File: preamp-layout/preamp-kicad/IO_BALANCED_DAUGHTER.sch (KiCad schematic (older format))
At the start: 49 parts, among them J29 XLR3, J30 XLR3, J31 Conn_01x03_Male, J32 Conn_01x03_Male, J33 Conn_01x03_Female, J34 Conn_01x03_Male, J35 XLR3, J36 XLR3, U6 TL072, U7 TL072, U8 TL072

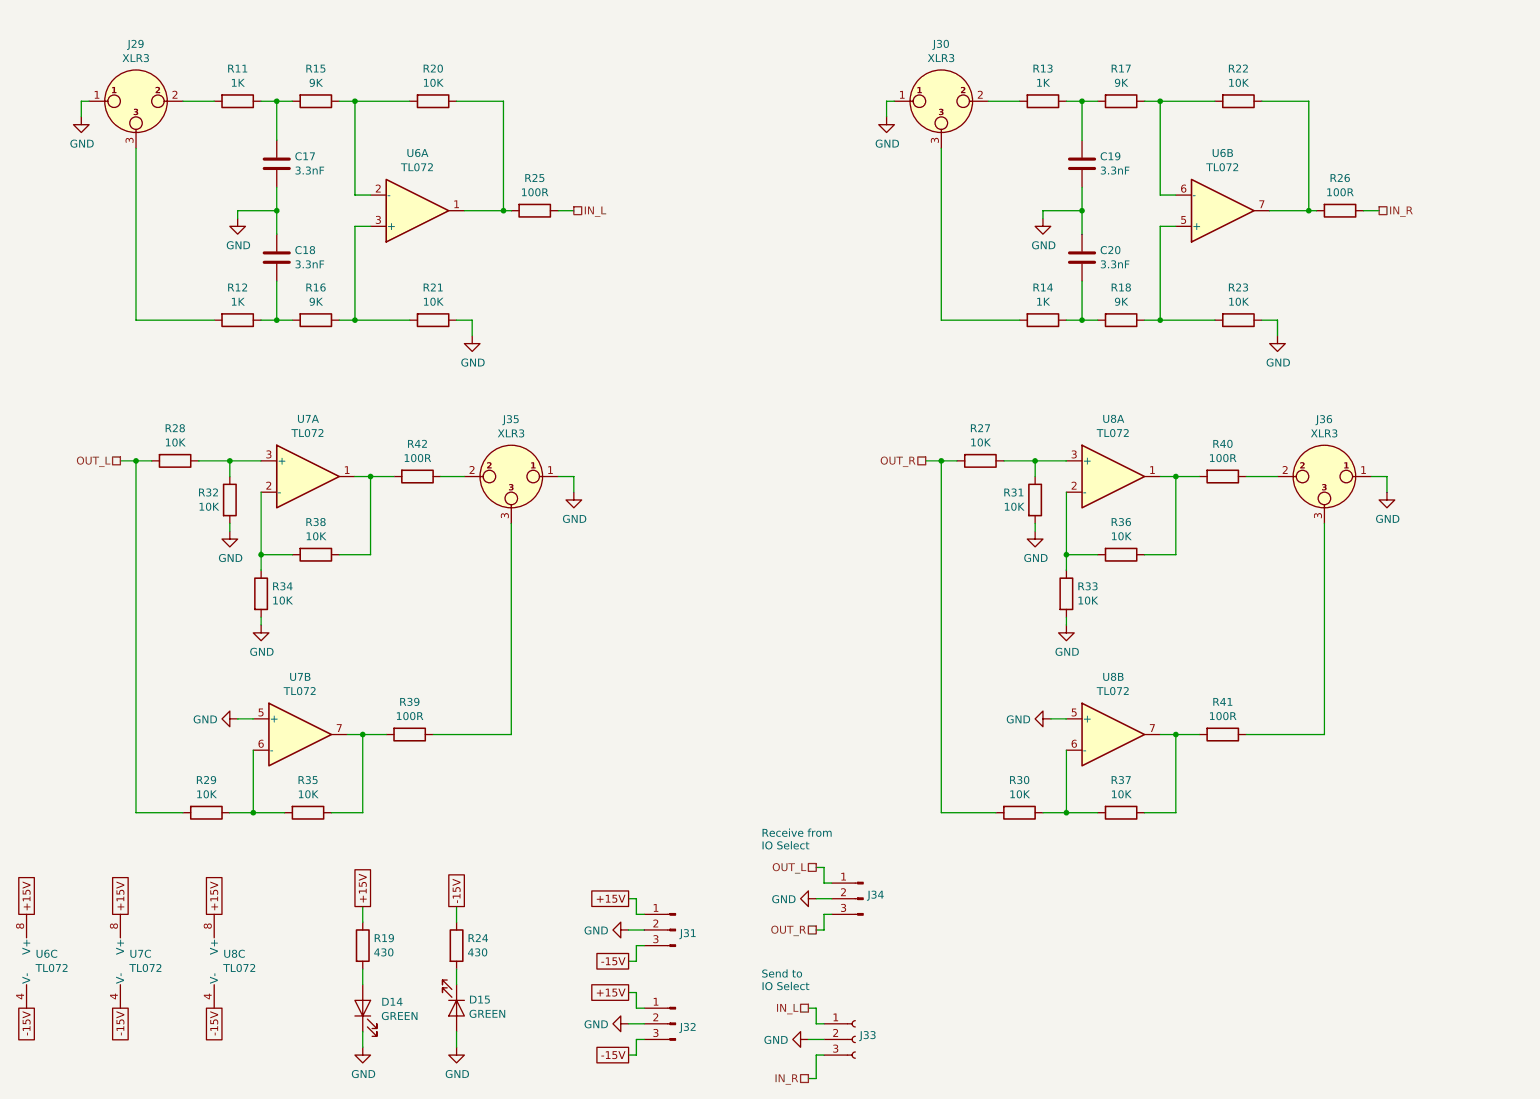
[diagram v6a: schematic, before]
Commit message: LED resistor update
In the process of reviewing layouts and associated parts sourcing, I realized that I had incorrectly calculated the resistors needed for the power supply LEDs on all boards. Updated BOM and schematics to match. Other minor schematic updates.
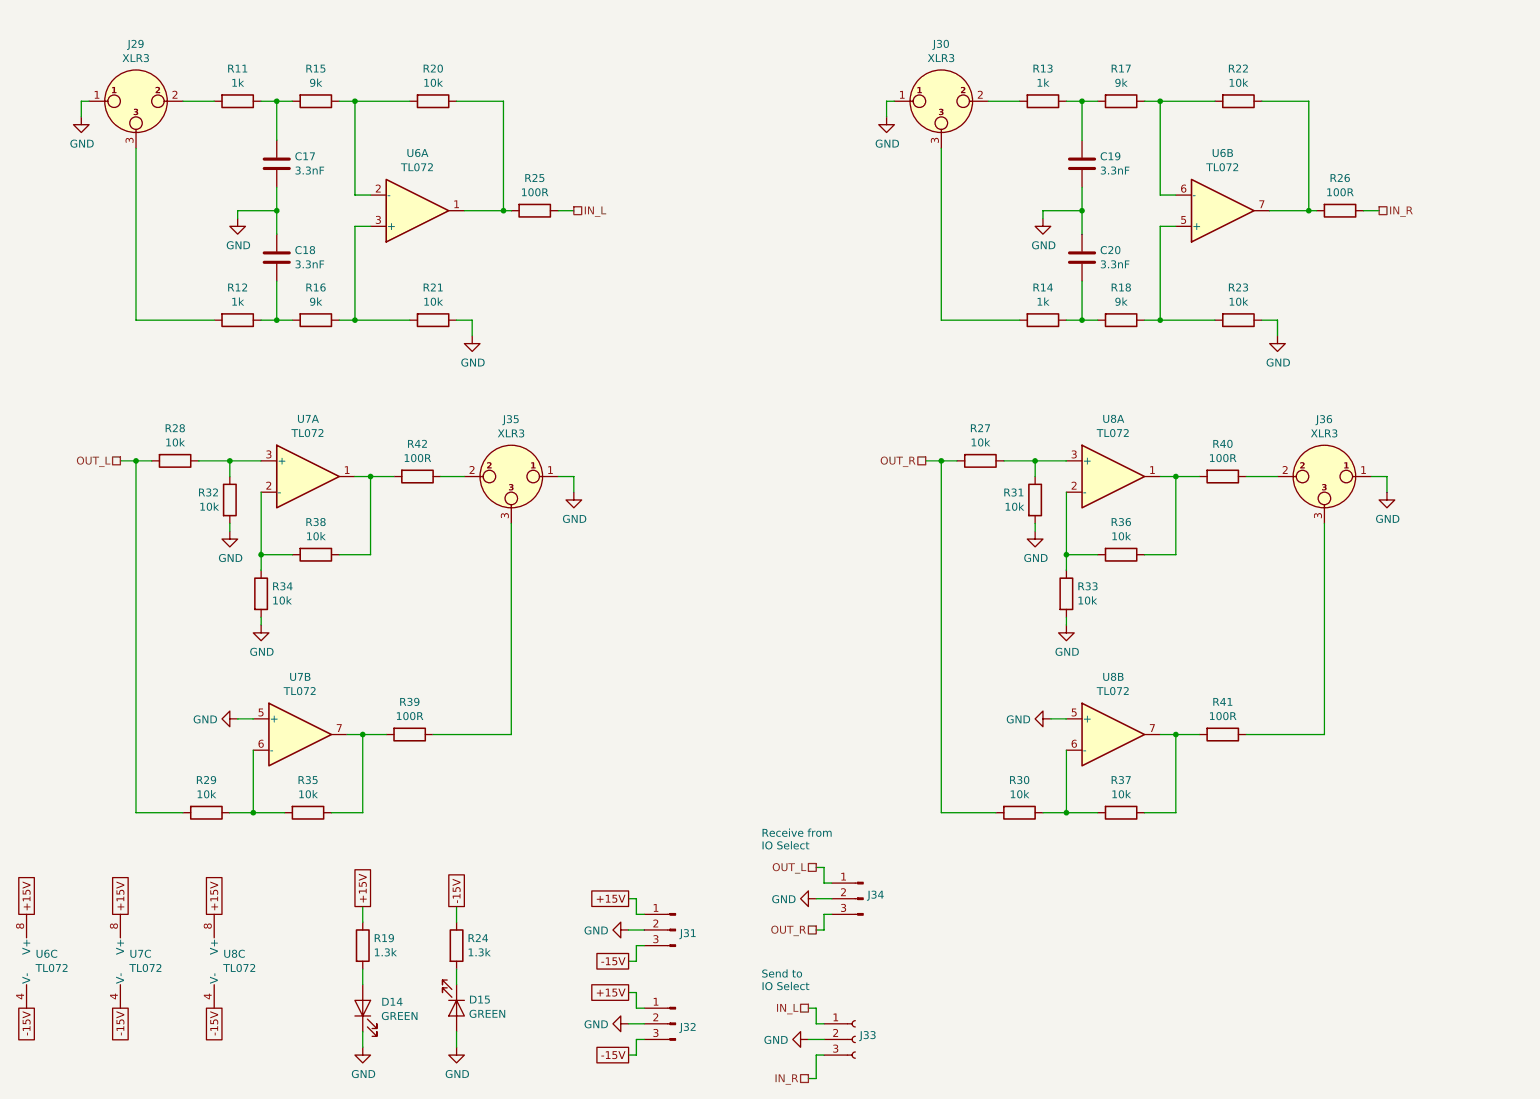
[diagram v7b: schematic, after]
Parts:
- R11, R12, R13, R14: value 1K -> 1k
- R15, R16, R17, R18: value 9K -> 9k
- R19, R24: value 430 -> 1.3k
- R20, R21, R22, R23, R27, R28, R29, R30, R31, R32, R33, R34, R35, R36, R37, R38: value 10K -> 10k
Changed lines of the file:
@@
 AR Path="/5E80BFEC/5E1BDDF0" Ref="R?"  Part="1"
 F 0 "R21" V 3493 2650 50  0000 C CNN
-F 1 "10K" V 3584 2650 50  0000 C CNN
+F 1 "10k" V 3584 2650 50  0000 C CNN
 F 2 "Resistor_SMD:R_1206_3216Metric_Pad1.42x1.75mm_HandSolder" V 3630 2650 50  0001 C CNN
 F 3 "~" H 3700 2650 50  0001 C CNN
@@
 AR Path="/5E80BFEC/5E1BDDF6" Ref="R?"  Part="1"
 F 0 "R20" V 3493 1250 50  0000 C CNN
-F 1 "10K" V 3584 1250 50  0000 C CNN
+F 1 "10k" V 3584 1250 50  0000 C CNN
 F 2 "Resistor_SMD:R_1206_3216Metric_Pad1.42x1.75mm_HandSolder" V 3630 1250 50  0001 C CNN
 F 3 "~" H 3700 1250 50  0001 C CNN
@@
 AR Path="/5E80BFEC/5E1BDE02" Ref="R?"  Part="1"
 F 0 "R16" V 2743 2650 50  0000 C CNN
-F 1 "9K" V 2834 2650 50  0000 C CNN
+F 1 "9k" V 2834 2650 50  0000 C CNN
 F 2 "Resistor_SMD:R_1206_3216Metric_Pad1.42x1.75mm_HandSolder" V 2880 2650 50  0001 C CNN
 F 3 "~" H 2950 2650 50  0001 C CNN
@@
 AR Path="/5E80BFEC/5E1BDE08" Ref="R?"  Part="1"
 F 0 "R12" V 2243 2650 50  0000 C CNN
-F 1 "1K" V 2334 2650 50  0000 C CNN
+F 1 "1k" V 2334 2650 50  0000 C CNN
 F 2 "Resistor_SMD:R_1206_3216Metric_Pad1.42x1.75mm_HandSolder" V 2380 2650 50  0001 C CNN
 F 3 "~" H 2450 2650 50  0001 C CNN
@@
 AR Path="/5E80BFEC/5E1BDE14" Ref="R?"  Part="1"
 F 0 "R11" V 2243 1250 50  0000 C CNN
-F 1 "1K" V 2334 1250 50  0000 C CNN
+F 1 "1k" V 2334 1250 50  0000 C CNN
 F 2 "Resistor_SMD:R_1206_3216Metric_Pad1.42x1.75mm_HandSolder" V 2380 1250 50  0001 C CNN
 F 3 "~" H 2450 1250 50  0001 C CNN
@@
 AR Path="/5E80BFEC/5E1BDE3B" Ref="R?"  Part="1"
 F 0 "R15" V 2743 1250 50  0000 C CNN
-F 1 "9K" V 2834 1250 50  0000 C CNN
+F 1 "9k" V 2834 1250 50  0000 C CNN
 F 2 "Resistor_SMD:R_1206_3216Metric_Pad1.42x1.75mm_HandSolder" V 2880 1250 50  0001 C CNN
 F 3 "~" H 2950 1250 50  0001 C CNN
@@
 AR Path="/5E80BFEC/5E1BDE63" Ref="R?"  Part="1"
 F 0 "R23" V 8643 2650 50  0000 C CNN
-F 1 "10K" V 8734 2650 50  0000 C CNN
+F 1 "10k" V 8734 2650 50  0000 C CNN
 F 2 "Resistor_SMD:R_1206_3216Metric_Pad1.42x1.75mm_HandSolder" V 8780 2650 50  0001 C CNN
 F 3 "~" H 8850 2650 50  0001 C CNN
@@
 AR Path="/5E80BFEC/5E1BDE69" Ref="R?"  Part="1"
 F 0 "R22" V 8643 1250 50  0000 C CNN
-F 1 "10K" V 8734 1250 50  0000 C CNN
+F 1 "10k" V 8734 1250 50  0000 C CNN
 F 2 "Resistor_SMD:R_1206_3216Metric_Pad1.42x1.75mm_HandSolder" V 8780 1250 50  0001 C CNN
 F 3 "~" H 8850 1250 50  0001 C CNN
@@
 AR Path="/5E80BFEC/5E1BDE75" Ref="R?"  Part="1"
 F 0 "R18" V 7893 2650 50  0000 C CNN
-F 1 "9K" V 7984 2650 50  0000 C CNN
+F 1 "9k" V 7984 2650 50  0000 C CNN
 F 2 "Resistor_SMD:R_1206_3216Metric_Pad1.42x1.75mm_HandSolder" V 8030 2650 50  0001 C CNN
 F 3 "~" H 8100 2650 50  0001 C CNN
@@
 AR Path="/5E80BFEC/5E1BDE7B" Ref="R?"  Part="1"
 F 0 "R14" V 7393 2650 50  0000 C CNN
-F 1 "1K" V 7484 2650 50  0000 C CNN
+F 1 "1k" V 7484 2650 50  0000 C CNN
 F 2 "Resistor_SMD:R_1206_3216Metric_Pad1.42x1.75mm_HandSolder" V 7530 2650 50  0001 C CNN
 F 3 "~" H 7600 2650 50  0001 C CNN
@@
 AR Path="/5E80BFEC/5E1BDE87" Ref="R?"  Part="1"
 F 0 "R13" V 7393 1250 50  0000 C CNN
-F 1 "1K" V 7484 1250 50  0000 C CNN
+F 1 "1k" V 7484 1250 50  0000 C CNN
 F 2 "Resistor_SMD:R_1206_3216Metric_Pad1.42x1.75mm_HandSolder" V 7530 1250 50  0001 C CNN
 F 3 "~" H 7600 1250 50  0001 C CNN
@@
 AR Path="/5E80BFEC/5E1BDE9E" Ref="R?"  Part="1"
 F 0 "R17" V 7893 1250 50  0000 C CNN
-F 1 "9K" V 7984 1250 50  0000 C CNN
+F 1 "9k" V 7984 1250 50  0000 C CNN
 F 2 "Resistor_SMD:R_1206_3216Metric_Pad1.42x1.75mm_HandSolder" V 8030 1250 50  0001 C CNN
 F 3 "~" H 8100 1250 50  0001 C CNN
@@
 AR Path="/5E80BFEC/5E1BDEC3" Ref="R?"  Part="1"
 F 0 "R29" V 2043 5800 50  0000 C CNN
-F 1 "10K" V 2134 5800 50  0000 C CNN
+F 1 "10k" V 2134 5800 50  0000 C CNN
 F 2 "Resistor_SMD:R_1206_3216Metric_Pad1.42x1.75mm_HandSolder" V 2180 5800 50  0001 C CNN
 F 3 "~" H 2250 5800 50  0001 C CNN
@@
 AR Path="/5E80BFEC/5E1BDEC9" Ref="R?"  Part="1"
 F 0 "R35" V 2693 5800 50  0000 C CNN
-F 1 "10K" V 2784 5800 50  0000 C CNN
+F 1 "10k" V 2784 5800 50  0000 C CNN
 F 2 "Resistor_SMD:R_1206_3216Metric_Pad1.42x1.75mm_HandSolder" V 2830 5800 50  0001 C CNN
 F 3 "~" H 2900 5800 50  0001 C CNN
@@
 AR Path="/5E80BFEC/5E1BDEF1" Ref="R?"  Part="1"
 F 0 "R32" H 2331 3846 50  0000 R CNN
-F 1 "10K" H 2331 3755 50  0000 R CNN
+F 1 "10k" H 2331 3755 50  0000 R CNN
 F 2 "Resistor_SMD:R_1206_3216Metric_Pad1.42x1.75mm_HandSolder" V 2330 3800 50  0001 C CNN
 F 3 "~" H 2400 3800 50  0001 C CNN
@@
 AR Path="/5E80BFEC/5E1BDEF7" Ref="R?"  Part="1"
 F 0 "R28" V 1843 3550 50  0000 C CNN
-F 1 "10K" V 1934 3550 50  0000 C CNN
+F 1 "10k" V 1934 3550 50  0000 C CNN
 F 2 "Resistor_SMD:R_1206_3216Metric_Pad1.42x1.75mm_HandSolder" V 1980 3550 50  0001 C CNN
 F 3 "~" H 2050 3550 50  0001 C CNN
@@
 Wire Wire Line
 	2400 3950 2400 4000
-$Comp
-L Device:R R?
-U 1 1 5E1BDF02
-P 3600 3650
-AR Path="/5E2D8DA2/5E1BDF02" Ref="R?"  Part="1"
-AR Path="/5E1BDF02" Ref="R?"  Part="1"
-AR Path="/5E1A0CE1/5E1BDF02" Ref="R42"  Part="1"
-AR Path="/5E80BFEC/5E1BDF02" Ref="R?"  Part="1"
-F 0 "R42" V 3393 3650 50  0000 C CNN
-F 1 "100R" V 3484 3650 50  0000 C CNN
-F 2 "Resistor_SMD:R_1206_3216Metric_Pad1.42x1.75mm_HandSolder" V 3530 3650 50  0001 C CNN
-F 3 "~" H 3600 3650 50  0001 C CNN
-	1    3600 3650
-	0    1    1    0
-$EndComp
 $Comp
 L Device:R R?
@@
 AR Path="/5E80BFEC/5E1BDF08" Ref="R?"  Part="1"
 F 0 "R38" V 2743 4150 50  0000 C CNN
-F 1 "10K" V 2834 4150 50  0000 C CNN
+F 1 "10k" V 2834 4150 50  0000 C CNN
 F 2 "Resistor_SMD:R_1206_3216Metric_Pad1.42x1.75mm_HandSolder" V 2880 4150 50  0001 C CNN
 F 3 "~" H 2950 4150 50  0001 C CNN
@@
 Wire Wire Line
 	2800 4150 2600 4150
-$Comp
-L Device:R R?
-U 1 1 5E1BDF16
-P 2600 4400
-AR Path="/5E2D8DA2/5E1BDF16" Ref="R?"  Part="1"
-AR Path="/5E1BDF16" Ref="R?"  Part="1"
-AR Path="/5E1A0CE1/5E1BDF16" Ref="R34"  Part="1"
-AR Path="/5E80BFEC/5E1BDF16" Ref="R?"  Part="1"
-F 0 "R34" H 2670 4446 50  0000 L CNN
-F 1 "10K" H 2670 4355 50  0000 L CNN
-F 2 "Resistor_SMD:R_1206_3216Metric_Pad1.42x1.75mm_HandSolder" V 2530 4400 50  0001 C CNN
-F 3 "~" H 2600 4400 50  0001 C CNN
-	1    2600 4400
-	1    0    0    -1
-$EndComp
 Wire Wire Line
 	2600 4550 2600 4600
@@
 AR Path="/5E80BFEC/5E1BDF33" Ref="R?"  Part="1"
 F 0 "R31" H 7481 3846 50  0000 R CNN
-F 1 "10K" H 7481 3755 50  0000 R CNN
+F 1 "10k" H 7481 3755 50  0000 R CNN
 F 2 "Resistor_SMD:R_1206_3216Metric_Pad1.42x1.75mm_HandSolder" V 7480 3800 50  0001 C CNN
 F 3 "~" H 7550 3800 50  0001 C CNN
@@
 AR Path="/5E80BFEC/5E1BDF39" Ref="R?"  Part="1"
 F 0 "R27" V 6993 3550 50  0000 C CNN
-F 1 "10K" V 7084 3550 50  0000 C CNN
+F 1 "10k" V 7084 3550 50  0000 C CNN
 F 2 "Resistor_SMD:R_1206_3216Metric_Pad1.42x1.75mm_HandSolder" V 7130 3550 50  0001 C CNN
 F 3 "~" H 7200 3550 50  0001 C CNN
@@
 AR Path="/5E80BFEC/5E1BDF4A" Ref="R?"  Part="1"
 F 0 "R36" V 7893 4150 50  0000 C CNN
-F 1 "10K" V 7984 4150 50  0000 C CNN
+F 1 "10k" V 7984 4150 50  0000 C CNN
 F 2 "Resistor_SMD:R_1206_3216Metric_Pad1.42x1.75mm_HandSolder" V 8030 4150 50  0001 C CNN
 F 3 "~" H 8100 4150 50  0001 C CNN
@@
 AR Path="/5E80BFEC/5E1BDF58" Ref="R?"  Part="1"
 F 0 "R33" H 7820 4446 50  0000 L CNN
-F 1 "10K" H 7820 4355 50  0000 L CNN
+F 1 "10k" H 7820 4355 50  0000 L CNN
 F 2 "Resistor_SMD:R_1206_3216Metric_Pad1.42x1.75mm_HandSolder" V 7680 4400 50  0001 C CNN
 F 3 "~" H 7750 4400 50  0001 C CNN
@@
 AR Path="/5E80BFEC/5E1BDF85" Ref="R?"  Part="1"
 F 0 "R30" V 7243 5800 50  0000 C CNN
-F 1 "10K" V 7334 5800 50  0000 C CNN
+F 1 "10k" V 7334 5800 50  0000 C CNN
 F 2 "Resistor_SMD:R_1206_3216Metric_Pad1.42x1.75mm_HandSolder" V 7380 5800 50  0001 C CNN
 F 3 "~" H 7450 5800 50  0001 C CNN
@@
 AR Path="/5E80BFEC/5E1BDF8B" Ref="R?"  Part="1"
 F 0 "R37" V 7893 5800 50  0000 C CNN
-F 1 "10K" V 7984 5800 50  0000 C CNN
+F 1 "10k" V 7984 5800 50  0000 C CNN
 F 2 "Resistor_SMD:R_1206_3216Metric_Pad1.42x1.75mm_HandSolder" V 8030 5800 50  0001 C CNN
 F 3 "~" H 8100 5800 50  0001 C CNN
@@
 AR Path="/5E80BFEC/5E50A27F" Ref="R?"  Part="1"
 F 0 "R19" H 3320 6696 50  0000 L CNN
-F 1 "430" H 3320 6605 50  0000 L CNN
+F 1 "1.3k" H 3320 6605 50  0000 L CNN
 F 2 "Resistor_SMD:R_1206_3216Metric_Pad1.42x1.75mm_HandSolder" V 3180 6650 50  0001 C CNN
 F 3 "~" H 3250 6650 50  0001 C CNN
@@
 AR Path="/5E80BFEC/5E50A28F" Ref="R?"  Part="1"
 F 0 "R24" H 3920 6696 50  0000 L CNN
-F 1 "430" H 3920 6605 50  0000 L CNN
+F 1 "1.3k" H 3920 6605 50  0000 L CNN
 F 2 "Resistor_SMD:R_1206_3216Metric_Pad1.42x1.75mm_HandSolder" V 3780 6650 50  0001 C CNN
 F 3 "~" H 3850 6650 50  0001 C CNN
@@
 	-1   0    0    -1
 $EndComp
+$Comp
+L Device:R R?
+U 1 1 5E1BDF02
+P 3600 3650
+AR Path="/5E2D8DA2/5E1BDF02" Ref="R?"  Part="1"
+AR Path="/5E1BDF02" Ref="R?"  Part="1"
+AR Path="/5E1A0CE1/5E1BDF02" Ref="R42"  Part="1"
+AR Path="/5E80BFEC/5E1BDF02" Ref="R?"  Part="1"
+F 0 "R42" V 3393 3650 50  0000 C CNN
+F 1 "100R" V 3484 3650 50  0000 C CNN
+F 2 "Resistor_SMD:R_1206_3216Metric_Pad1.42x1.75mm_HandSolder" V 3530 3650 50  0001 C CNN
+F 3 "~" H 3600 3650 50  0001 C CNN
+	1    3600 3650
+	0    1    1    0
+$EndComp
+$Comp
+L Device:R R?
+U 1 1 5E1BDF16
+P 2600 4400
+AR Path="/5E2D8DA2/5E1BDF16" Ref="R?"  Part="1"
+AR Path="/5E1BDF16" Ref="R?"  Part="1"
+AR Path="/5E1A0CE1/5E1BDF16" Ref="R34"  Part="1"
+AR Path="/5E80BFEC/5E1BDF16" Ref="R?"  Part="1"
+F 0 "R34" H 2670 4446 50  0000 L CNN
+F 1 "10k" H 2670 4355 50  0000 L CNN
+F 2 "Resistor_SMD:R_1206_3216Metric_Pad1.42x1.75mm_HandSolder" V 2530 4400 50  0001 C CNN
+F 3 "~" H 2600 4400 50  0001 C CNN
+	1    2600 4400
+	1    0    0    -1
+$EndComp
 $EndSCHEMATC

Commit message: Initial Review
Reviewing schematic, comparing to references and filling in BOM to match schematics. Updating footprints in the process as well.
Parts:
- C17, C18, C19, C20: footprint (none) -> Capacitor_SMD:C_0805_2012Metric_Pad1.15x1.40mm_HandSolder
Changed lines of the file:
@@
 F 0 "C18" H 2815 2296 50  0000 L CNN
 F 1 "3.3nF" H 2815 2205 50  0000 L CNN
-F 2 "" H 2738 2100 50  0001 C CNN
+F 2 "Capacitor_SMD:C_0805_2012Metric_Pad1.15x1.40mm_HandSolder" H 2738 2100 50  0001 C CNN
 F 3 "~" H 2700 2250 50  0001 C CNN
 	1    2700 2250
@@
 F 0 "C17" H 2815 1696 50  0000 L CNN
 F 1 "3.3nF" H 2815 1605 50  0000 L CNN
-F 2 "" H 2738 1500 50  0001 C CNN
+F 2 "Capacitor_SMD:C_0805_2012Metric_Pad1.15x1.40mm_HandSolder" H 2738 1500 50  0001 C CNN
 F 3 "~" H 2700 1650 50  0001 C CNN
 	1    2700 1650
@@
 F 0 "C20" H 7965 2296 50  0000 L CNN
 F 1 "3.3nF" H 7965 2205 50  0000 L CNN
-F 2 "" H 7888 2100 50  0001 C CNN
+F 2 "Capacitor_SMD:C_0805_2012Metric_Pad1.15x1.40mm_HandSolder" H 7888 2100 50  0001 C CNN
 F 3 "~" H 7850 2250 50  0001 C CNN
 	1    7850 2250
@@
 F 0 "C19" H 7965 1696 50  0000 L CNN
 F 1 "3.3nF" H 7965 1605 50  0000 L CNN
-F 2 "" H 7888 1500 50  0001 C CNN
+F 2 "Capacitor_SMD:C_0805_2012Metric_Pad1.15x1.40mm_HandSolder" H 7888 1500 50  0001 C CNN
 F 3 "~" H 7850 1650 50  0001 C CNN
 	1    7850 1650
